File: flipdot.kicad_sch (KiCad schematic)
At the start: 43 parts, among them J1 Conn_01x06_Pin, U1 74HC595

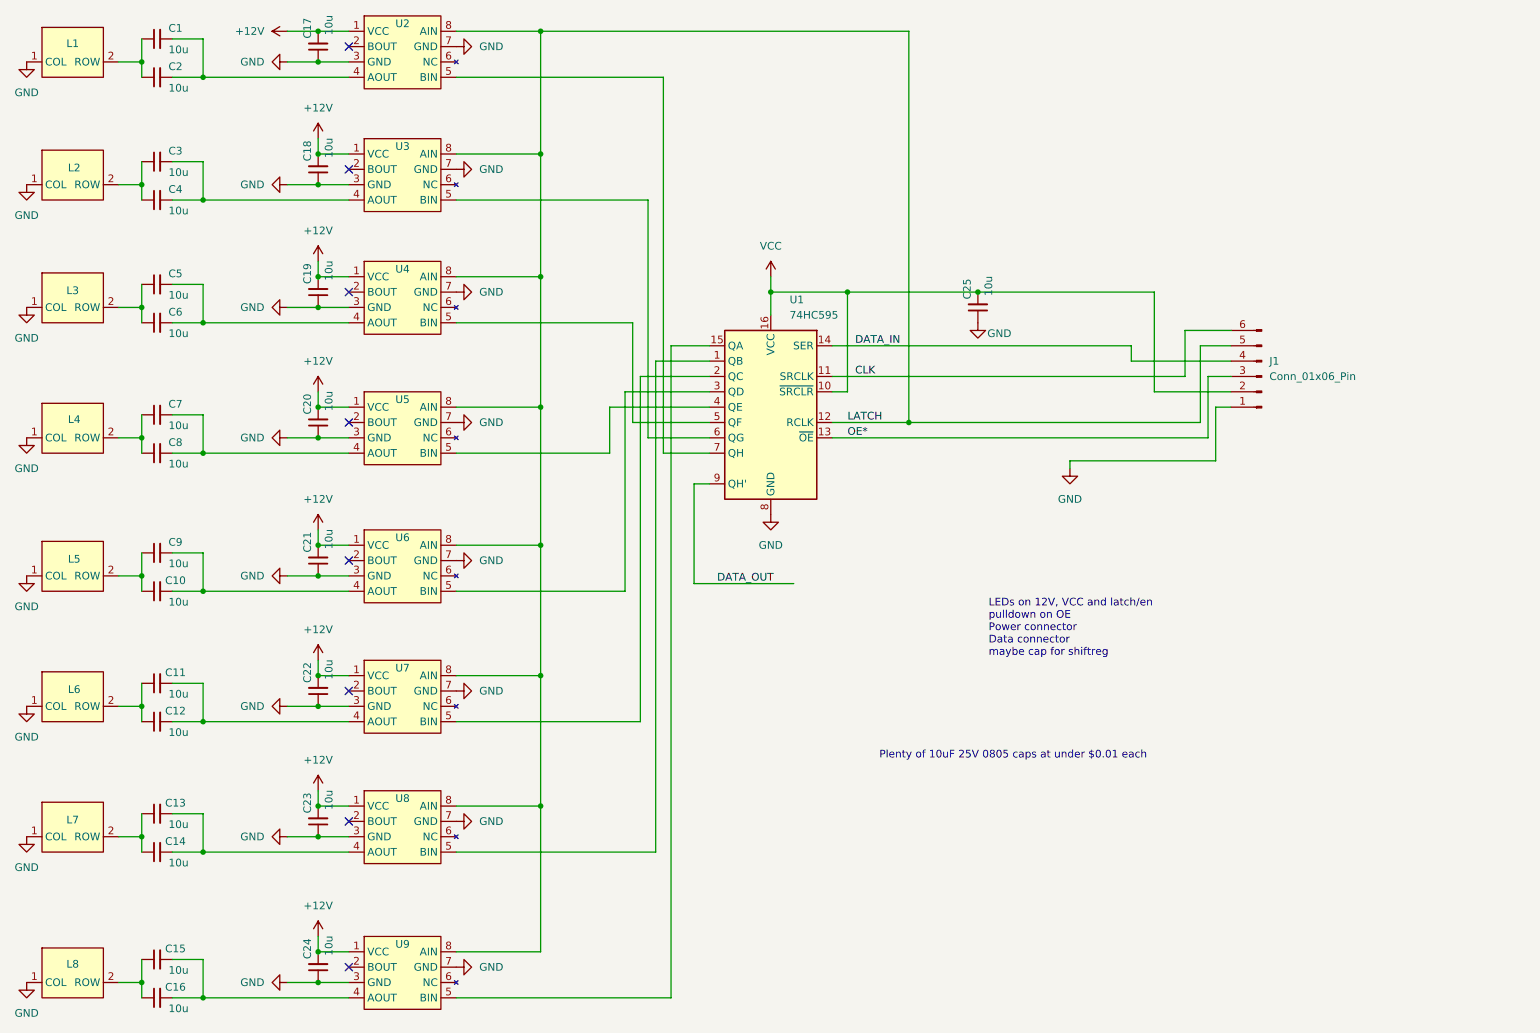
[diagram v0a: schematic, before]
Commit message: use JST ZH
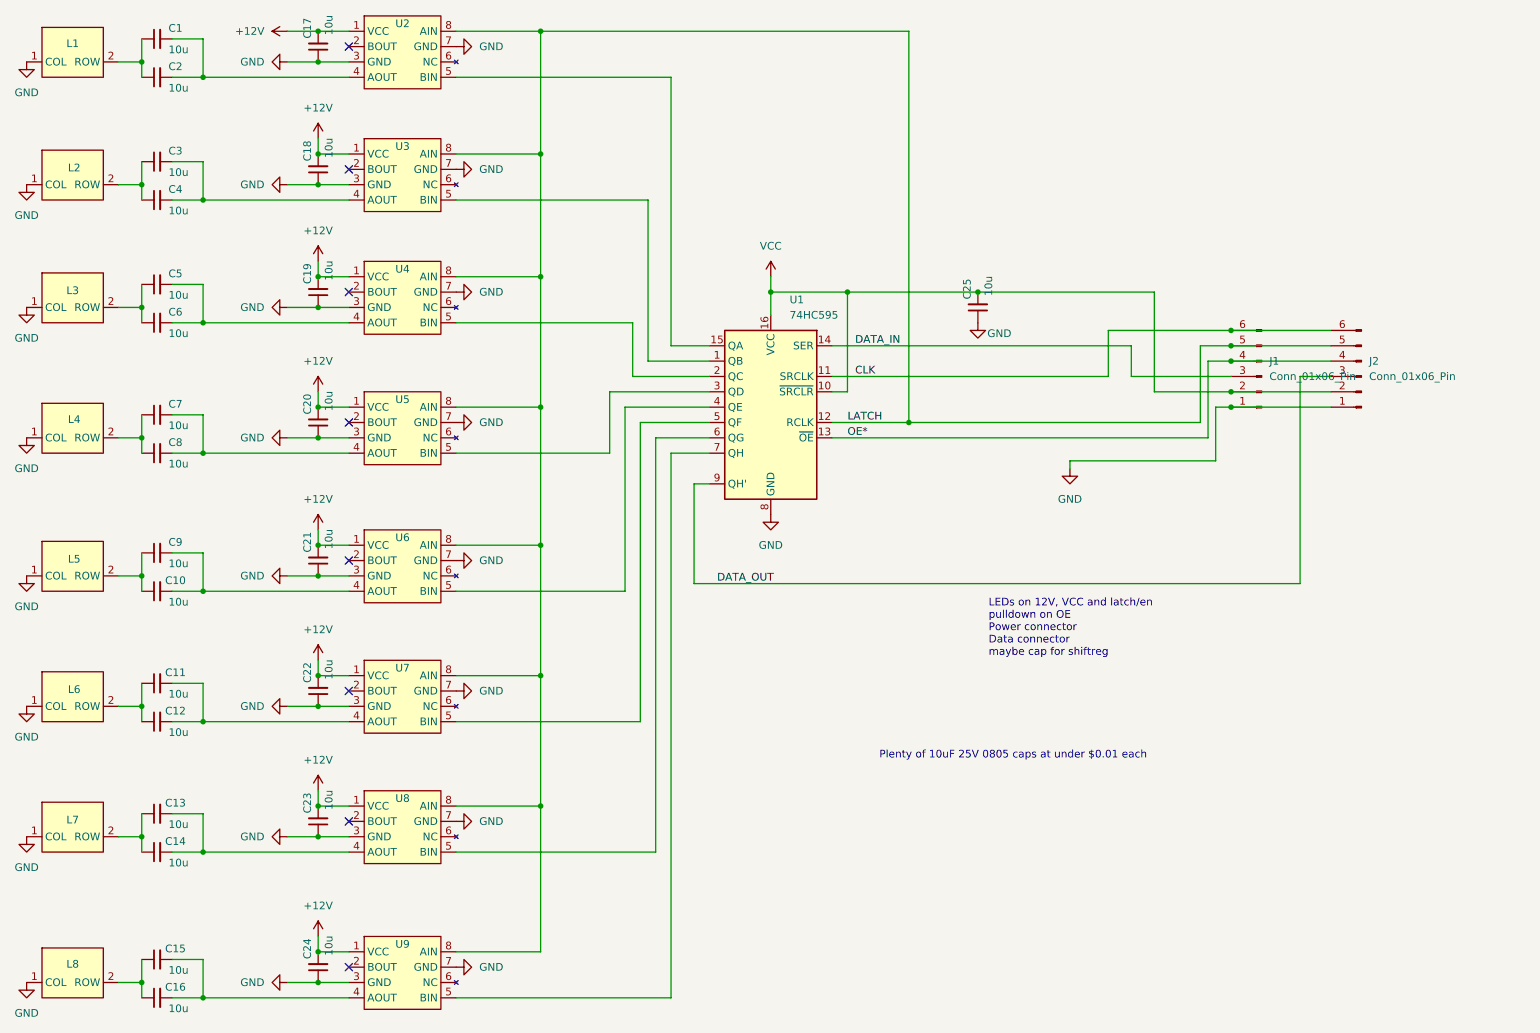
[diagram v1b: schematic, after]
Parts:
- added J2: Conn_01x06_Pin, Connector_JST:JST_ZH_B6B-ZR_1x06_P1.50mm_Vertical, symbol Connector:Conn_01x06_Pin
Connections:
- net CLK: now also J2.6 (Pin_6)
- net DATA_IN: now also J1.3 (Pin_3); no longer J1.4 (Pin_4)
- net DATA_OUT: now also J2.3 (Pin_3)
- net GND: now also J2.1 (Pin_1)
- net LATCH: now also J2.5 (Pin_5)
- net OE*: now also J1.4 (Pin_4), J2.4 (Pin_4); no longer J1.3 (Pin_3)
- net VCC: now also J2.2 (Pin_2)
- net at U2.5 (BIN): now also U1.15 (QA); no longer U1.7 (QH)
- net at U1.1 (QB): now also U3.5 (BIN); no longer U8.5 (BIN)
- net at U9.5 (BIN): now also U1.7 (QH); no longer U1.15 (QA)
- net at U1.2 (QC): now also U4.5 (BIN); no longer U7.5 (BIN)
- net at U1.3 (QD): now also U5.5 (BIN); no longer U6.5 (BIN)
- net at U1.4 (QE): now also U6.5 (BIN); no longer U5.5 (BIN)
- net at U1.5 (QF): now also U7.5 (BIN); no longer U4.5 (BIN)
- net at U1.6 (QG): now also U8.5 (BIN); no longer U3.5 (BIN)

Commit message: flip everything again
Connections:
- net at U2.5 (BIN): now also U1.7 (QH); no longer U1.15 (QA)
- net at U1.1 (QB): now also U8.5 (BIN); no longer U3.5 (BIN)
- net at U1.2 (QC): now also U7.5 (BIN); no longer U4.5 (BIN)
- net at U1.3 (QD): now also U6.5 (BIN); no longer U5.5 (BIN)
- net at U1.4 (QE): now also U5.5 (BIN); no longer U6.5 (BIN)
- net at U1.5 (QF): now also U4.5 (BIN); no longer U7.5 (BIN)
- net at U1.6 (QG): now also U3.5 (BIN); no longer U8.5 (BIN)
- net at U9.5 (BIN): now also U1.15 (QA); no longer U1.7 (QH)
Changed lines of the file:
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@@
-	(wire
-		(pts
-			(xy 121.92 88.9) (xy 135.89 88.9)
-		)
-		(stroke
-			(width 0)
-			(type default)
-		)
-	)
 	(wire
 		(pts
@@
 	(wire
 		(pts
+			(xy 127 81.28) (xy 127 162.56)
+		)
+		(stroke
+			(width 0)
+			(type default)
+		)
+	)
+	(wire
+		(pts
 			(xy 38.1 72.39) (xy 41.91 72.39)
 		)
@@
 	(wire
 		(pts
-			(xy 218.44 81.28) (xy 218.44 93.98)
+			(xy 215.9 81.28) (xy 215.9 93.98)
 		)
 		(stroke
@@
 	(wire
 		(pts
+			(xy 128.27 34.29) (xy 128.27 96.52)
+		)
+		(stroke
+			(width 0)
+			(type default)
+		)
+	)
+	(wire
+		(pts
 			(xy 222.25 76.2) (xy 238.76 76.2)
 		)
@@
 	(wire
 		(pts
+			(xy 129.54 78.74) (xy 135.89 78.74)
+		)
+		(stroke
+			(width 0)
+			(type default)
+		)
+	)
+	(wire
+		(pts
 			(xy 41.91 93.98) (xy 41.91 96.52)
 		)
@@
 	(wire
 		(pts
-			(xy 168.91 91.44) (xy 217.17 91.44)
+			(xy 168.91 91.44) (xy 213.36 91.44)
 		)
 		(stroke
@@
 	(wire
 		(pts
-			(xy 217.17 78.74) (xy 222.25 78.74)
+			(xy 213.36 78.74) (xy 222.25 78.74)
 		)
 		(stroke
@@
 	(wire
 		(pts
-			(xy 129.54 96.52) (xy 129.54 186.69)
-		)
-		(stroke
-			(width 0)
-			(type default)
-		)
-	)
-	(wire
-		(pts
 			(xy 195.58 99.06) (xy 195.58 97.79)
 		)
@@
 	(wire
 		(pts
+			(xy 121.92 86.36) (xy 121.92 119.38)
+		)
+		(stroke
+			(width 0)
+			(type default)
+		)
+	)
+	(wire
+		(pts
 			(xy 46.99 140.97) (xy 52.07 140.97)
 		)
@@
 	(wire
 		(pts
-			(xy 218.44 81.28) (xy 222.25 81.28)
+			(xy 215.9 81.28) (xy 222.25 81.28)
 		)
 		(stroke
@@
 	(wire
 		(pts
-			(xy 119.38 86.36) (xy 119.38 96.52)
-		)
-		(stroke
-			(width 0)
-			(type default)
-		)
-	)
-	(wire
-		(pts
 			(xy 46.99 113.03) (xy 52.07 113.03)
 		)
@@
 	(wire
 		(pts
-			(xy 219.71 88.9) (xy 222.25 88.9)
+			(xy 218.44 88.9) (xy 222.25 88.9)
 		)
 		(stroke
@@
 	(wire
 		(pts
-			(xy 124.46 91.44) (xy 135.89 91.44)
-		)
-		(stroke
-			(width 0)
-			(type default)
-		)
-	)
-	(wire
-		(pts
 			(xy 222.25 86.36) (xy 238.76 86.36)
 		)
@@
 	(wire
 		(pts
-			(xy 217.17 91.44) (xy 217.17 78.74)
+			(xy 213.36 91.44) (xy 213.36 78.74)
 		)
 		(stroke
@@
 	(wire
 		(pts
+			(xy 121.92 86.36) (xy 135.89 86.36)
+		)
+		(stroke
+			(width 0)
+			(type default)
+		)
+	)
+	(wire
+		(pts
 			(xy 156.21 78.74) (xy 205.74 78.74)
 		)
@@
 	(wire
 		(pts
-			(xy 123.19 83.82) (xy 135.89 83.82)
-		)
-		(stroke
-			(width 0)
-			(type default)
-		)
-	)
-	(wire
-		(pts
 			(xy 76.2 154.94) (xy 71.12 154.94)
 		)
@@
 	(wire
 		(pts
+			(xy 127 81.28) (xy 135.89 81.28)
+		)
+		(stroke
+			(width 0)
+			(type default)
+		)
+	)
+	(wire
+		(pts
 			(xy 46.99 74.93) (xy 52.07 74.93)
 		)
@@
 	(wire
 		(pts
-			(xy 125.73 54.61) (xy 125.73 81.28)
+			(xy 125.73 54.61) (xy 125.73 93.98)
 		)
 		(stroke
@@
 	(wire
 		(pts
-			(xy 156.21 93.98) (xy 218.44 93.98)
+			(xy 156.21 93.98) (xy 215.9 93.98)
 		)
 		(stroke
@@
 	(wire
 		(pts
+			(xy 124.46 83.82) (xy 135.89 83.82)
+		)
+		(stroke
+			(width 0)
+			(type default)
+		)
+	)
+	(wire
+		(pts
 			(xy 52.07 140.97) (xy 76.2 140.97)
 		)
@@
 	(wire
 		(pts
-			(xy 93.98 34.29) (xy 129.54 34.29)
+			(xy 93.98 34.29) (xy 128.27 34.29)
 		)
 		(stroke
@@
 	(wire
 		(pts
-			(xy 119.38 86.36) (xy 135.89 86.36)
-		)
-		(stroke
-			(width 0)
-			(type default)
-		)
-	)
-	(wire
-		(pts
 			(xy 76.2 88.9) (xy 71.12 88.9)
 		)
@@
 	(wire
 		(pts
-			(xy 127 93.98) (xy 135.89 93.98)
-		)
-		(stroke
-			(width 0)
-			(type default)
-		)
-	)
-	(wire
-		(pts
 			(xy 46.99 34.29) (xy 52.07 34.29)
 		)
@@
 	(wire
 		(pts
+			(xy 129.54 78.74) (xy 129.54 186.69)
+		)
+		(stroke
+			(width 0)
+			(type default)
+		)
+	)
+	(wire
+		(pts
 			(xy 76.2 46.99) (xy 71.12 46.99)
 		)
@@
 	(wire
 		(pts
-			(xy 124.46 91.44) (xy 124.46 140.97)
+			(xy 124.46 83.82) (xy 124.46 140.97)
+		)
+		(stroke
+			(width 0)
+			(type default)
+		)
+	)
+	(wire
+		(pts
+			(xy 119.38 88.9) (xy 119.38 96.52)
 		)
 		(stroke
@@
 	(wire
 		(pts
-			(xy 129.54 78.74) (xy 135.89 78.74)
-		)
-		(stroke
-			(width 0)
-			(type default)
-		)
-	)
-	(wire
-		(pts
 			(xy 52.07 156.21) (xy 52.07 162.56)
 		)
@@
 	(wire
 		(pts
-			(xy 121.92 88.9) (xy 121.92 119.38)
-		)
-		(stroke
-			(width 0)
-			(type default)
-		)
-	)
-	(wire
-		(pts
 			(xy 133.35 118.11) (xy 233.68 118.11)
 		)
@@
 	(wire
 		(pts
-			(xy 195.58 97.79) (xy 219.71 97.79)
+			(xy 195.58 97.79) (xy 218.44 97.79)
 		)
 		(stroke
@@
 	(wire
 		(pts
-			(xy 129.54 96.52) (xy 135.89 96.52)
+			(xy 123.19 91.44) (xy 135.89 91.44)
 		)
 		(stroke
@@
 	(wire
 		(pts
-			(xy 127 93.98) (xy 127 162.56)
+			(xy 119.38 88.9) (xy 135.89 88.9)
 		)
 		(stroke
@@
 	(wire
 		(pts
-			(xy 123.19 74.93) (xy 123.19 83.82)
+			(xy 128.27 96.52) (xy 135.89 96.52)
+		)
+		(stroke
+			(width 0)
+			(type default)
+		)
+	)
+	(wire
+		(pts
+			(xy 123.19 74.93) (xy 123.19 91.44)
 		)
 		(stroke
@@
 	(wire
 		(pts
-			(xy 219.71 97.79) (xy 219.71 88.9)
+			(xy 218.44 97.79) (xy 218.44 88.9)
 		)
 		(stroke
@@
 	(wire
 		(pts
-			(xy 125.73 81.28) (xy 135.89 81.28)
-		)
-		(stroke
-			(width 0)
-			(type default)
-		)
-	)
-	(wire
-		(pts
 			(xy 52.07 186.69) (xy 76.2 186.69)
 		)
@@
 	(wire
 		(pts
-			(xy 129.54 34.29) (xy 129.54 78.74)
-		)
-		(stroke
-			(width 0)
-			(type default)
-		)
-	)
-	(wire
-		(pts
 			(xy 205.74 83.82) (xy 222.25 83.82)
 		)
@@
 		)
 		(stroke
+			(width 0)
+			(type default)
+		)
+	)
+	(wire
+		(pts
+			(xy 125.73 93.98) (xy 135.89 93.98)
+		)
+		(stroke

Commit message: some progress
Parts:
- added J3, J4, J5: Conn_01x02_Pin, Connector_JST:JST_VH_B2P-VH_1x02_P3.96mm_Vertical, symbol Connector:Conn_01x02_Pin
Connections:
- net +12V: now also J3.1 (Pin_1), J4.1 (Pin_1), J5.1 (Pin_1)
- net GND: now also J3.2 (Pin_2), J4.2 (Pin_2), J5.2 (Pin_2)

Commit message: mounting holes
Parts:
- removed J5: Conn_01x02_Pin, Connector_JST:JST_VH_B2P-VH_1x02_P3.96mm_Vertical, symbol Connector:Conn_01x02_Pin
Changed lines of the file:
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@@
-	)
-	(symbol
-		(lib_id "power:+12V")
-		(at 260.35 44.45 270)
-		(unit 1)
-		(exclude_from_sim no)
-		(in_bom yes)
-		(on_board yes)
-		(dnp no)
-		(fields_autoplaced yes)
-		(property "Reference" "#PWR041"
-			(at 256.54 44.45 0)
-			(effects
-				(font
-					(size 1.27 1.27)
-				)
-				(hide yes)
-			)
-		)
-		(property "Value" "+12V"
-			(at 264.16 44.4499 90)
-			(effects
-				(font
-					(size 1.27 1.27)
-				)
-				(justify left)
-			)
-		)
-		(property "Footprint" ""
-			(at 260.35 44.45 0)
-			(effects
-				(font
-					(size 1.27 1.27)
-				)
-				(hide yes)
-			)
-		)
-		(property "Datasheet" ""
-			(at 260.35 44.45 0)
-			(effects
-				(font
-					(size 1.27 1.27)
-				)
-				(hide yes)
-			)
-		)
-		(property "Description" "Power symbol creates a global label with name \"+12V\""
-			(at 260.35 44.45 0)
-			(effects
-				(font
-					(size 1.27 1.27)
-				)
-				(hide yes)
-			)
-		)
-		(pin "1"
-		)
-		(instances
-			(project "flipdot"
-				(path "/2f7734fa-ef95-48ac-9211-21614044c9f8"
-					(reference "#PWR041")
-					(unit 1)
-				)
-			)
-		)
 	)
 	(symbol
@@
 	)
 	(symbol
-		(lib_id "Connector:Conn_01x02_Pin")
-		(at 255.27 44.45 0)
-		(unit 1)
-		(exclude_from_sim no)
-		(in_bom yes)
-		(on_board yes)
-		(dnp no)
-		(fields_autoplaced yes)
-		(property "Reference" "J5"
-			(at 255.905 39.37 0)
-			(effects
-				(font
-					(size 1.27 1.27)
-				)
-			)
-		)
-		(property "Value" "Conn_01x02_Pin"
-			(at 255.905 41.91 0)
-			(effects
-				(font
-					(size 1.27 1.27)
-				)
-			)
-		)
-		(property "Footprint" "Connector_JST:JST_VH_B2P-VH_1x02_P3.96mm_Vertical"
-			(at 255.27 44.45 0)
-			(effects
-				(font
-					(size 1.27 1.27)
-				)
-				(hide yes)
-			)
-		)
-		(property "Datasheet" "~"
-			(at 255.27 44.45 0)
-			(effects
-				(font
-					(size 1.27 1.27)
-				)
-				(hide yes)
-			)
-		)
-		(property "Description" "Generic connector, single row, 01x02, script generated"
-			(at 255.27 44.45 0)
-			(effects
-				(font
-					(size 1.27 1.27)
-				)
-				(hide yes)
-			)
-		)
-		(pin "2"
-		)
-		(pin "1"
-		)
-		(instances
-			(project "flipdot"
-				(path "/2f7734fa-ef95-48ac-9211-21614044c9f8"
-					(reference "J5")
-					(unit 1)
-				)
-			)
-		)
-	)
-	(symbol
 		(lib_id "power:GND")
 		(at 93.98 69.85 90)
@@
 					(unit 1)
 				)
-			)
-		)
-	)
-	(symbol
-		(lib_id "power:GND")
-		(at 260.35 46.99 90)
-		(unit 1)
-		(exclude_from_sim no)
-		(in_bom yes)
-		(on_board yes)
-		(dnp no)
-		(fields_autoplaced yes)
-		(property "Reference" "#PWR042"
-			(at 266.7 46.99 0)
-			(effects
-				(font
-					(size 1.27 1.27)
-				)
-				(hide yes)
-			)
-		)
-		(property "Value" "GND"
-			(at 264.16 46.9899 90)
-			(effects
-				(font
-					(size 1.27 1.27)
-				)
-				(justify right)
-			)
-		)
-		(property "Footprint" ""
-			(at 260.35 46.99 0)
-			(effects
-				(font
-					(size 1.27 1.27)
-				)
-				(hide yes)
-			)
-		)
-		(property "Datasheet" ""
-			(at 260.35 46.99 0)
-			(effects
-				(font
-					(size 1.27 1.27)
-				)
-				(hide yes)
-			)
-		)
-		(property "Description" "Power symbol creates a global label with name \"GND\" , ground"
-			(at 260.35 46.99 0)
-			(effects
-				(font
-					(size 1.27 1.27)
-				)
-				(hide yes)
-			)
-		)
-		(pin "1"
-		)
-		(instances
-			(project "flipdot"
-				(path "/2f7734fa-ef95-48ac-9211-21614044c9f8"
-					(reference "#PWR042")
-					(unit 1)
-				)

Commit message: fatten 12v line
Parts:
- added J5: Conn_01x02_Pin, Connector_JST:JST_VH_B2P-VH_1x02_P3.96mm_Vertical, symbol Connector:Conn_01x02_Pin
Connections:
- net +12V: now also J5.1 (Pin_1)
- net GND: now also J5.2 (Pin_2)
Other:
- note added: "LEDs on 12V, VCC and latch/en pulldown on OE add SMD 12v pads"
- note removed: "LEDs on 12V, VCC and latch/en pulldown on OE Power connector Data connector maybe cap for shiftreg"
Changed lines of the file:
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@@
 		)
 	)
-	(text "LEDs on 12V, VCC and latch/en\npulldown on OE\nPower connector\nData connector\nmaybe cap for shiftreg"
+	(text "LEDs on 12V, VCC and latch/en\npulldown on OE\nadd SMD 12v pads\n"
 		(exclude_from_sim no)
 		(at 182.118 125.476 0)
@@
 	)
 	(symbol
+		(lib_id "power:GND")
+		(at 261.62 46.99 90)
+		(unit 1)
+		(exclude_from_sim no)
+		(in_bom yes)
+		(on_board yes)
+		(dnp no)
+		(fields_autoplaced yes)
+		(property "Reference" "#PWR042"
+			(at 267.97 46.99 0)
+			(effects
+				(font
+					(size 1.27 1.27)
+				)
+				(hide yes)
+			)
+		)
+		(property "Value" "GND"
+			(at 265.43 46.9899 90)
+			(effects
+				(font
+					(size 1.27 1.27)
+				)
+				(justify right)
+			)
+		)
+		(property "Footprint" ""
+			(at 261.62 46.99 0)
+			(effects
+				(font
+					(size 1.27 1.27)
+				)
+				(hide yes)
+			)
+		)
+		(property "Datasheet" ""
+			(at 261.62 46.99 0)
+			(effects
+				(font
+					(size 1.27 1.27)
+				)
+				(hide yes)
+			)
+		)
+		(property "Description" "Power symbol creates a global label with name \"GND\" , ground"
+			(at 261.62 46.99 0)
+			(effects
+				(font
+					(size 1.27 1.27)
+				)
+				(hide yes)
+			)
+		)
+		(pin "1"
+		)
+		(instances
+			(project "flipdot"
+				(path "/2f7734fa-ef95-48ac-9211-21614044c9f8"
+					(reference "#PWR042")
+					(unit 1)
+				)
+			)
+		)
+	)
+	(symbol
 		(lib_id "Device:C_Small")
 		(at 71.12 181.61 180)
@@
 	)
 	(symbol
+		(lib_id "Connector:Conn_01x02_Pin")
+		(at 256.54 44.45 0)
+		(unit 1)
+		(exclude_from_sim no)
+		(in_bom yes)
+		(on_board yes)
+		(dnp no)
+		(fields_autoplaced yes)
+		(property "Reference" "J5"
+			(at 257.175 39.37 0)
+			(effects
+				(font
+					(size 1.27 1.27)
+				)
+			)
+		)
+		(property "Value" "Conn_01x02_Pin"
+			(at 257.175 41.91 0)
+			(effects
+				(font
+					(size 1.27 1.27)
+				)
+			)
+		)
+		(property "Footprint" "Connector_JST:JST_VH_B2P-VH_1x02_P3.96mm_Vertical"
+			(at 256.54 44.45 0)
+			(effects
+				(font
+					(size 1.27 1.27)
+				)
+				(hide yes)
+			)
+		)
+		(property "Datasheet" "~"
+			(at 256.54 44.45 0)
+			(effects
+				(font
+					(size 1.27 1.27)
+				)
+				(hide yes)
+			)
+		)
+		(property "Description" "Generic connector, single row, 01x02, script generated"
+			(at 256.54 44.45 0)
+			(effects
+				(font
+					(size 1.27 1.27)
+				)
+				(hide yes)
+			)
+		)
+		(pin "2"
+		)
+		(pin "1"
+		)
+		(instances
+			(project "flipdot"
+				(path "/2f7734fa-ef95-48ac-9211-21614044c9f8"
+					(reference "J5")
+					(unit 1)
+				)
+			)
+		)
+	)
+	(symbol
 		(lib_id "Device:C_Small")
 		(at 44.45 68.58 90)
@@
 					(unit 1)
 				)
+			)
+		)
+	)
+	(symbol
+		(lib_id "power:+12V")
+		(at 261.62 44.45 270)
+		(unit 1)
+		(exclude_from_sim no)
+		(in_bom yes)
+		(on_board yes)
+		(dnp no)
+		(fields_autoplaced yes)
+		(property "Reference" "#PWR041"
+			(at 257.81 44.45 0)
+			(effects
+				(font
+					(size 1.27 1.27)
+				)
+				(hide yes)
+			)
+		)
+		(property "Value" "+12V"
+			(at 265.43 44.4499 90)
+			(effects
+				(font
+					(size 1.27 1.27)
+				)
+				(justify left)
+			)
+		)
+		(property "Footprint" ""
+			(at 261.62 44.45 0)
+			(effects
+				(font
+					(size 1.27 1.27)
+				)
+				(hide yes)
+			)
+		)
+		(property "Datasheet" ""
+			(at 261.62 44.45 0)
+			(effects
+				(font
+					(size 1.27 1.27)
+				)
+				(hide yes)
+			)
+		)
+		(property "Description" "Power symbol creates a global label with name \"+12V\""
+			(at 261.62 44.45 0)
+			(effects
+				(font
+					(size 1.27 1.27)
+				)
+				(hide yes)
+			)
+		)
+		(pin "1"
+		)
+		(instances
+			(project "flipdot"
+				(path "/2f7734fa-ef95-48ac-9211-21614044c9f8"
+					(reference "#PWR041")
+					(unit 1)
+				)

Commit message: single row mostly complete
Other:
- note added: "LEDs on 12V, VCC and latch/en pulldown on OE"
- note removed: "LEDs on 12V, VCC and latch/en pulldown on OE add SMD 12v pads"
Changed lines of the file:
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@@
 		)
 	)
-	(text "LEDs on 12V, VCC and latch/en\npulldown on OE\nadd SMD 12v pads\n"
+	(text "LEDs on 12V, VCC and latch/en\npulldown on OE\n\n"
 		(exclude_from_sim no)
 		(at 182.118 125.476 0)
